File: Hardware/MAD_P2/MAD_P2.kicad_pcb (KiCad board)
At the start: 2 copper layers, 121.6 x 145.5 mm, 363 parts, among them J1 Line_1_3, J10 Conn_02x05_Odd_Even, J11 Conn_02x05_Odd_Even, J12 Line_3_3, J13 Conn_02x05_Odd_Even, J14 Conn_02x05_Odd_Even, J15 Conn_ADC1, J16 Conn_DAC, J17 Line_1_2, J18 P3, J19 P4, J2 Line_2_2, J20 P2, J21 Conn_02x05_Odd_Even, J22 Conn_02x05_Odd_Even, J23 Conn_02x03_Odd_Even, J24 P5, J25 P6, J26 P7, J27 Line_1_1, J28 Line_2_1, J29 Line_2_3, J3 Line_3_1, J30 Line_3_2, J31 Micro_SD_Card_Connector, J32 Micro_SD_Card_Socket, J33 Shifted IO, J4 Power_In, J5 Micro_SD_Card, J6 Edge_Conn, J7 Conn_02x05_Odd_Even, J8 USB_C_Receptacle_USB2.0, J9 Conn_02x05_Odd_Even, P10 CONN_01X01, P11 CONN_01X01, P13 CONN_01X01, P8 CONN_01X01, Q1 MMBT3904, Q2 2N7002, Q3 2N7002, Q4 2N7002, Q5 2N7002, SW1 Switch_SW_Push, U1 P2X8C4M64P-REF, U10 AMS1117-3.3, U11 APM4953, U12 APM4953, U13 XL1509-5.0, U14 XL1509-5.0, U15 AMS1117-3.3, U16 AMS1117-3.3, U17 MAX5134-7, U18 AMS1117-3.3, U19 AMS1117-1.8, U2 XL1509-5.0, U20 LM321, U21 APM4953, U22 XL1509-5.0, U23 ADS131A04, U24 AMS1117-3.3, U26 W25Q128JVS, U27 FT232RL, U28 DS3231M, U29 ESP-12F, U3 XL1509-5.0, U4 XL1509-5.0, U5 XL1509-5.0, U6 AMS1117-3.3, U7 AMS1117-3.3, U8 AMS1117-3.3, U9 AMS1117-3.3, Y1 20MHz, Y2 16.384MHz

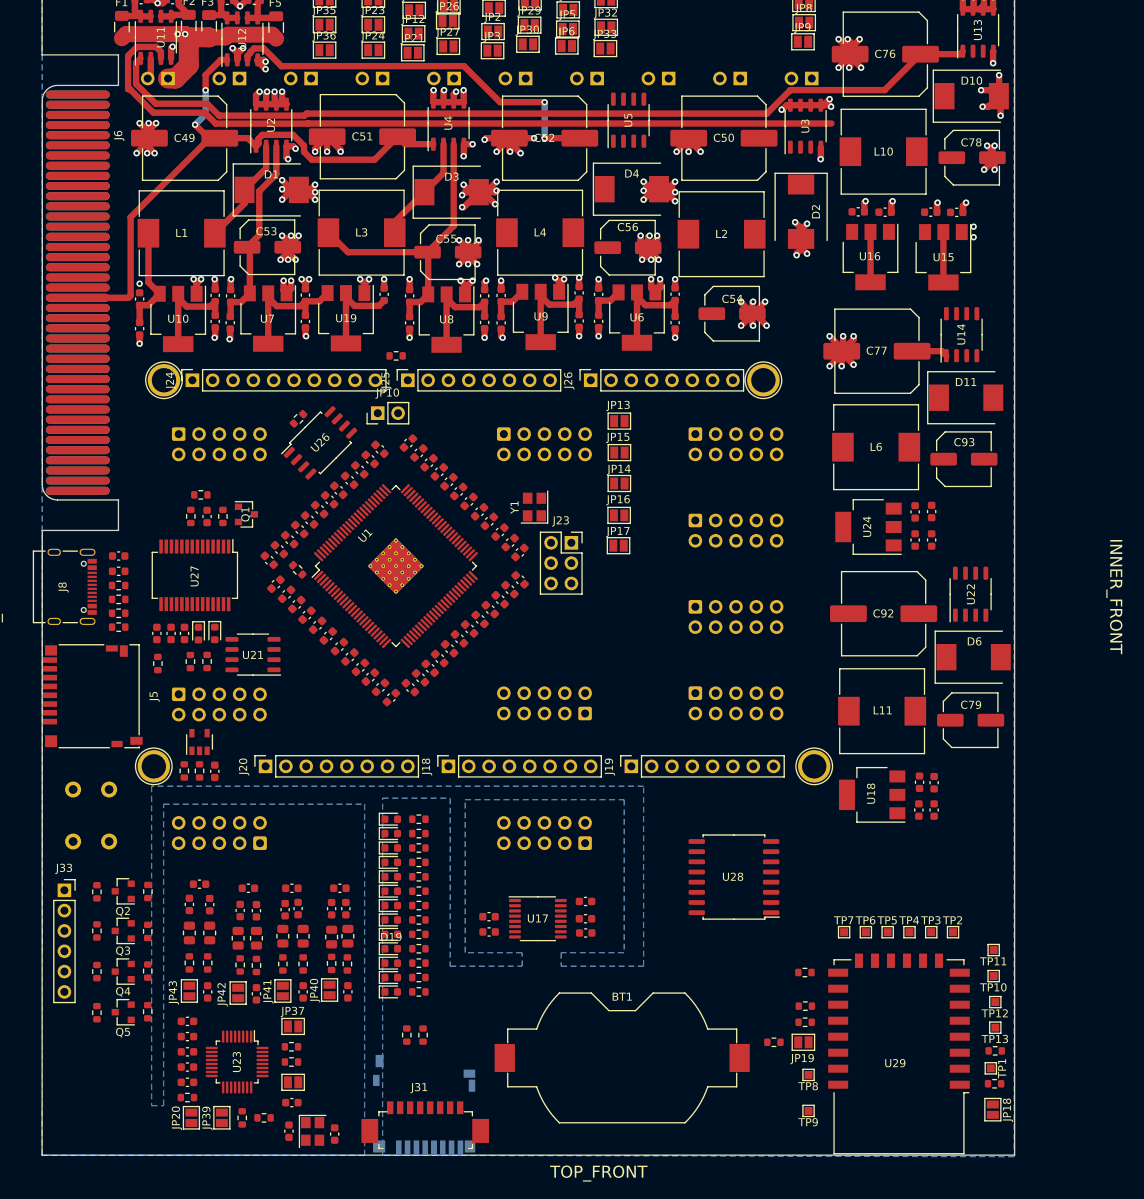
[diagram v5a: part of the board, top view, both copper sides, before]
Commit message: routed adc
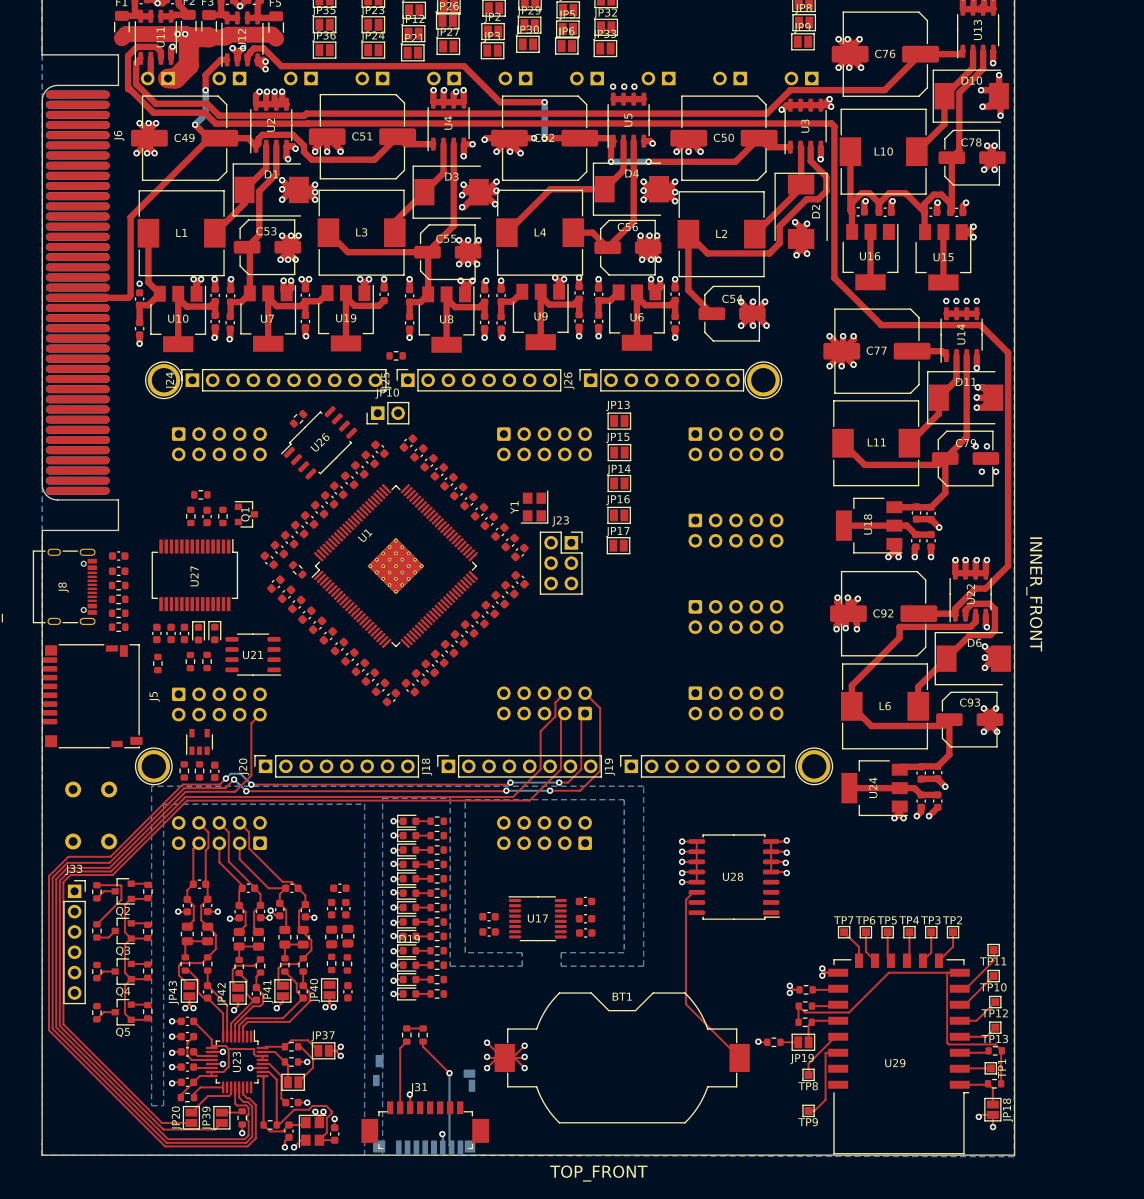
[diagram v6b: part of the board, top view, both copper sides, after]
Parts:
- moved C82 33.7 mm to (501.6, 84.1)
- moved C83 33.7 mm to (501.7, 80.6)
- moved C86 33.7 mm to (503.6, 84.1)
- moved C87 33.7 mm to (503.6, 80.7)
- moved U18 33.7 mm to (495.8, 82.2)
- moved L11 33.5 mm to (496.7, 71.9)
- moved C79 32.7 mm to (507.9, 73.8)
- moved C100 32.6 mm to (504.4, 116.6)
- moved C101 32.6 mm to (502.3, 116.6)
- moved C95 32.6 mm to (504.4, 113.1)
- moved C97 32.6 mm to (502.3, 113.1)
- moved U24 32.6 mm to (496.5, 115.0)
- moved C93 32.6 mm to (508.4, 106.4)
- moved L6 32.4 mm to (497.8, 104.8)
- moved JP37 4.88 mm to (427.6, 147.8)
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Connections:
- net /Connections/P64 renamed Net-(J11-Pad1)
- net D+ renamed /Connections/D+
- net D- renamed /Connections/D-
- C1 pad 1: /V_0_3 -> V_0_3
- C10 pad 1: /V_36_39 -> V_32_35
- C13 pad 1: /V_8_11 -> V_0_3
- C14 pad 1: /V_8_11 -> V_0_3
- C15 pad 1: /V_40_43 -> V_32_35
- C16 pad 1: /V_40_43 -> V_32_35
- C19 pad 1: /V_12_15 -> V_0_3
- C2 pad 1: /V_0_3 -> V_0_3
- C20 pad 1: /V_12_15 -> V_0_3
- C21 pad 1: /V_44_47 -> V_32_35
- C22 pad 1: /V_44_47 -> V_32_35
- C25 pad 1: /V_16_19 -> V_0_3
- C26 pad 1: /V_16_19 -> V_0_3
- C27 pad 1: /V_48_51 -> V_32_35
- C28 pad 1: /V_48_51 -> V_32_35
- C3 pad 1: /V_32_35 -> V_32_35
- C31 pad 1: /V_20_23 -> V_0_3
- C32 pad 1: /V_20_23 -> V_0_3
- C33 pad 1: /V_52_55 -> V_32_35
- C34 pad 1: /V_52_55 -> V_32_35
- C37 pad 1: /V_24_27 -> V_0_3
- C38 pad 1: /V_24_27 -> V_0_3
- C39 pad 1: /V_56_59 -> V_32_35
- C4 pad 1: /V_32_35 -> V_32_35
- C40 pad 1: /V_56_59 -> V_32_35
- C43 pad 1: /V_28_31 -> V_0_3
- C44 pad 1: /V_28_31 -> V_0_3
- C45 pad 1: /V_60_63 -> V_32_35
- C46 pad 1: /V_60_63 -> V_32_35
- C7 pad 1: /V_4_7 -> V_0_3
- C8 pad 1: /V_4_7 -> V_0_3
- C9 pad 1: /V_36_39 -> V_32_35
- J10 pad 1: /Connections/P54 -> P54
- J10 pad 10: /Connections/P63 -> P63
- J10 pad 2: /Connections/P55 -> P55
- J10 pad 3: /Connections/P56 -> P56
- J10 pad 4: /Connections/P57 -> P57
- J10 pad 5: /Connections/P58 -> P58
- J10 pad 6: /Connections/P59 -> P59
- J10 pad 7: /Connections/P60 -> P60
- J10 pad 8: /Connections/P61 -> P61
- J10 pad 9: /Connections/P62 -> P62
- J11 pad 2: /Connections/V_0_3 -> V_0_3
- J11 pad 3: /Connections/V_16_19 -> V_0_3
- J11 pad 4: /Connections/V_32_35 -> V_32_35
- J11 pad 5: /Connections/V_48_51 -> V_32_35
- J13 pad 1: /Connections/P20 -> P20
- J13 pad 10: /Connections/P29 -> P29
- J13 pad 2: /Connections/P21 -> P21
- J13 pad 3: /Connections/P22 -> P22
- J13 pad 4: /Connections/P23 -> P23
- J13 pad 5: /Connections/P24 -> P24
- J13 pad 6: /Connections/P25 -> P25
- J13 pad 7: /Connections/P26 -> P26
- J13 pad 8: /Connections/P27 -> P27
- J13 pad 9: /Connections/P28 -> P28
- J16 pad 10: /Connections/A03 -> AO3
- J16 pad 2: /Connections/A01 -> AO1
- J16 pad 5: /Connections/A02 -> AO2
- J21 pad 1: /Connections/P0 -> P0
- J21 pad 10: /Connections/P9 -> P9
- J21 pad 2: /Connections/P1 -> P1
- J21 pad 3: /Connections/P2 -> P2
- J21 pad 4: /Connections/P3 -> P3
- J21 pad 5: /Connections/P4 -> P4
- J21 pad 6: /Connections/P5 -> P5
- J21 pad 7: /Connections/P6 -> P6
- J21 pad 8: /Connections/P7 -> P7
- J21 pad 9: /Connections/P8 -> P8
- J22 pad 1: /Connections/P10 -> P10
- J22 pad 10: /Connections/P19 -> P19
- J22 pad 2: /Connections/P11 -> P11
- J22 pad 3: /Connections/P12 -> P12
- J22 pad 4: /Connections/P13 -> P13
- J22 pad 5: /Connections/P14 -> P14
- J22 pad 6: /Connections/P15 -> P15
- J22 pad 7: /Connections/P16 -> P16
- J22 pad 8: /Connections/P17 -> P17
- J22 pad 9: /Connections/P18 -> P18
- J23 pad 2: /Connections/P53 -> P53
- J23 pad 3: /Connections/P52 -> P52
- J23 pad 4: /Connections/P51 -> P51
- J24 pad 8: /Connections/P55 -> P55
- J24 pad 9: /Connections/P54 -> P54
- J26 pad 7: /Connections/P57 -> P57
- J26 pad 8: /Connections/P56 -> P56
- J31 pad 2: /Connections/P42 -> P42
- J31 pad 3: /Connections/P41 -> P41
- J31 pad 5: /Connections/P40 -> P40
- J32 pad 2: /Connections/P42 -> P42
- J32 pad 3: /Connections/P41 -> P41
- J32 pad 5: /Connections/P40 -> P40
- J5 pad 2: /Memory/P60 -> P60
- J5 pad 3: /Memory/P59 -> P59
- J5 pad 5: /Memory/P61 -> P61
- J6 pad 10: /Connections/P30 -> P30
- J6 pad 11: /Connections/P29 -> P29
- J6 pad 12: /Connections/P28 -> P28
- J6 pad 13: /Connections/P27 -> P27
- J6 pad 14: /Connections/P26 -> P26
- J6 pad 15: /Connections/P25 -> P25
- J6 pad 16: /Connections/P24 -> P24
- J6 pad 17: /Connections/P23 -> P23
- J6 pad 18: /Connections/P22 -> P22
- J6 pad 19: /Connections/P21 -> P21
- J6 pad 20: /Connections/P20 -> P20
- J6 pad 21: /Connections/P19 -> P19
- J6 pad 22: /Connections/P18 -> P18
- J6 pad 23: /Connections/P17 -> P17
- J6 pad 24: /Connections/P16 -> P16
- J6 pad 25: /Connections/P15 -> P15
- J6 pad 26: /Connections/P14 -> P14
- J6 pad 27: /Connections/P13 -> P13
- J6 pad 28: /Connections/P12 -> P12
- J6 pad 29: /Connections/P11 -> P11
- J6 pad 3: /Connections/P37 -> P37
- J6 pad 30: /Connections/P10 -> P10
- J6 pad 31: /Connections/P9 -> P9
- J6 pad 32: /Connections/P8 -> P8
- J6 pad 33: /Connections/P7 -> P7
- J6 pad 34: /Connections/P6 -> P6
- J6 pad 35: /Connections/P5 -> P5
- J6 pad 36: /Connections/P4 -> P4
- J6 pad 37: /Connections/P3 -> P3
- J6 pad 38: /Connections/P2 -> P2
- J6 pad 39: /Connections/P1 -> P1
- J6 pad 4: /Connections/P36 -> P36
- J6 pad 40: /Connections/P0 -> P0
- J6 pad 47: /Connections/V_0_3 -> V_0_3
- J6 pad 48: /Connections/V_8_11 -> V_0_3
- J6 pad 49: /Connections/P63 -> P63
- J6 pad 5: /Connections/P35 -> P35
- J6 pad 50: /Connections/P62 -> P62
- J6 pad 51: /Connections/P61 -> P61
- J6 pad 52: /Connections/P60 -> P60
- J6 pad 53: /Connections/P59 -> P59
- J6 pad 54: /Connections/P58 -> P58
- J6 pad 55: /Connections/P57 -> P57
- J6 pad 56: /Connections/P56 -> P56
- J6 pad 57: /Connections/V_56_59 -> V_32_35
- J6 pad 58: /Connections/V_16_19 -> V_0_3
- J6 pad 59: /Connections/P55 -> P55
- J6 pad 6: /Connections/P34 -> P34
- J6 pad 60: /Connections/P54 -> P54
- J6 pad 61: /Connections/P53 -> P53
- J6 pad 62: /Connections/P52 -> P52
- J6 pad 63: /Connections/P51 -> P51
- J6 pad 64: /Connections/P50 -> P50
- J6 pad 65: /Connections/P49 -> P49
- J6 pad 66: /Connections/P48 -> P48
- J6 pad 67: /Connections/V_48_51 -> V_32_35
- J6 pad 68: /Connections/V_24_27 -> V_0_3
- J6 pad 69: /Connections/P47 -> P47
- J6 pad 7: /Connections/P33 -> P33
- J6 pad 70: /Connections/P46 -> P46
- J6 pad 71: /Connections/P45 -> P45
- J6 pad 72: /Connections/P44 -> P44
- J6 pad 73: /Connections/P43 -> P43
- J6 pad 74: /Connections/P42 -> P42
- J6 pad 75: /Connections/P41 -> P41
- J6 pad 76: /Connections/P40 -> P40
- J6 pad 77: /Connections/V_40_43 -> V_32_35
- J6 pad 78: /Connections/V_32_35 -> V_32_35
- J6 pad 79: /Connections/P39 -> P39
- J6 pad 8: /Connections/P32 -> P32
- J6 pad 80: /Connections/P38 -> P38
- J6 pad 9: /Connections/P31 -> P31
- J7 pad 1: /Connections/P34 -> P34
- J7 pad 10: /Connections/P43 -> P43
- J7 pad 2: /Connections/P35 -> P35
- J7 pad 3: /Connections/P36 -> P36
- J7 pad 4: /Connections/P37 -> P37
- J7 pad 5: /Connections/P38 -> P38
- J7 pad 6: /Connections/P39 -> P39
- J7 pad 7: /Connections/P40 -> P40
- J7 pad 8: /Connections/P41 -> P41
- J7 pad 9: /Connections/P42 -> P42
- J9 pad 1: /Connections/P44 -> P44
- J9 pad 10: /Connections/P53 -> P53
- J9 pad 2: /Connections/P45 -> P45
- J9 pad 3: /Connections/P46 -> P46
- J9 pad 4: /Connections/P47 -> P47
- J9 pad 5: /Connections/P48 -> P48
- J9 pad 6: /Connections/P49 -> P49
- J9 pad 7: /Connections/P50 -> P50
- J9 pad 8: /Connections/P51 -> P51
- J9 pad 9: /Connections/P52 -> P52
- JP10 pad 2: /Memory/P61 -> P61
- JP13 pad 2: /Connections/P30 -> P30
- JP14 pad 2: /Connections/P32 -> P32
- JP15 pad 1: /Connections/P31 -> P31
- JP16 pad 2: /Connections/P33 -> P33
- JP17 pad 1: /Connections/P34 -> P34
- JP20 pad 2: /Peripherals/P46 -> P46
- JP39 pad 2: /Peripherals/P47 -> P47
- Q2 pad 2: /Peripherals/P51 -> P51
- Q3 pad 2: /Peripherals/P52 -> P52
- Q4 pad 2: /Peripherals/P53 -> P53
- Q5 pad 2: /Peripherals/P54 -> P54
- R11 pad 1: /Memory/P58 -> P58
- R18 pad 2: /Connections/P63 -> P63
- R19 pad 1: /Connections/P62 -> P62
- R2 pad 1: /V_56_59 -> V_32_35
- R2 pad 2: /RESET -> RESET
- R35 pad 1: /Connections/P39 -> P39
- R36 pad 1: /Connections/P39 -> P39
- R38 pad 2: /Peripherals/P51 -> P51
- R43 pad 2: /Peripherals/P52 -> P52
- R48 pad 2: /Peripherals/P53 -> P53
- R50 pad 2: /Peripherals/P54 -> P54
- SW1 pad 1: /RESET -> RESET
- U1 pad 10: /P5 -> P5
- U1 pad 100: /RESET -> RESET
- U1 pad 11: /V_4_7 -> V_0_3
- U1 pad 12: /P6 -> P6
- U1 pad 13: /P7 -> P7
- U1 pad 15: /P8 -> P8
- U1 pad 16: /P9 -> P9
- U1 pad 17: /V_8_11 -> V_0_3
- U1 pad 18: /P10 -> P10
- U1 pad 19: /P11 -> P11
- U1 pad 21: /P12 -> P12
- U1 pad 22: /P13 -> P13
- U1 pad 23: /V_12_15 -> V_0_3
- U1 pad 24: /P14 -> P14
- U1 pad 25: /P15 -> P15
- U1 pad 27: /P16 -> P16
- U1 pad 28: /P17 -> P17
- U1 pad 29: /V_16_19 -> V_0_3
- U1 pad 3: /P0 -> P0
- U1 pad 30: /P18 -> P18
- U1 pad 31: /P19 -> P19
- U1 pad 33: /P20 -> P20
- U1 pad 34: /P21 -> P21
- U1 pad 35: /V_20_23 -> V_0_3
- U1 pad 36: /P22 -> P22
- U1 pad 37: /P23 -> P23
- U1 pad 39: /P24 -> P24
- U1 pad 4: /P1 -> P1
- U1 pad 40: /P25 -> P25
- U1 pad 41: /V_24_27 -> V_0_3
- U1 pad 42: /P26 -> P26
- U1 pad 43: /P27 -> P27
- U1 pad 45: /P28 -> P28
- U1 pad 46: /P29 -> P29
- U1 pad 47: /V_28_31 -> V_0_3
- U1 pad 48: /P30 -> P30
- U1 pad 49: /P31 -> P31
- U1 pad 5: /V_0_3 -> V_0_3
- U1 pad 53: /P32 -> P32
- U1 pad 54: /P33 -> P33
- U1 pad 55: /V_32_35 -> V_32_35
- U1 pad 56: /P34 -> P34
- U1 pad 57: /P35 -> P35
- U1 pad 59: /P36 -> P36
- U1 pad 6: /P2 -> P2
- U1 pad 60: /P37 -> P37
- U1 pad 61: /V_36_39 -> V_32_35
- U1 pad 62: /P38 -> P38
- U1 pad 63: /P39 -> P39
- U1 pad 65: /P40 -> P40
- U1 pad 66: /P41 -> P41
- U1 pad 67: /V_40_43 -> V_32_35
- U1 pad 68: /P42 -> P42
- U1 pad 69: /P43 -> P43
- U1 pad 7: /P3 -> P3
- U1 pad 71: /P44 -> P44
- U1 pad 72: /P45 -> P45
- U1 pad 73: /V_44_47 -> V_32_35
- U1 pad 74: /P46 -> P46
- U1 pad 75: /P47 -> P47
- U1 pad 77: /P48 -> P48
- U1 pad 78: /P49 -> P49
- U1 pad 79: /V_48_51 -> V_32_35
- U1 pad 80: /P50 -> P50
- U1 pad 81: /P51 -> P51
- U1 pad 83: /P52 -> P52
- U1 pad 84: /P53 -> P53
- U1 pad 85: /V_52_55 -> V_32_35
- U1 pad 86: /P54 -> P54
- U1 pad 87: /P55 -> P55
- U1 pad 89: /P56 -> P56
- U1 pad 9: /P4 -> P4
- U1 pad 90: /P57 -> P57
- U1 pad 91: /V_56_59 -> V_32_35
- U1 pad 92: /P58 -> P58
- U1 pad 93: /P59 -> P59
- U1 pad 95: /P60 -> P60
- U1 pad 96: /P61 -> P61
- U1 pad 97: /V_60_63 -> V_32_35
- U1 pad 98: /P62 -> P62
- U1 pad 99: /P63 -> P63
- U15 pad 2: /Power2/V_0_3 -> V_0_3
- U16 pad 2: /Power2/V_16_19 -> V_32_35
- U17 pad 10: /Peripherals/P49 -> P49
- U17 pad 11: /Peripherals/A02 -> AO2
- U17 pad 14: /Peripherals/A01 -> AO1
- U17 pad 6: /Peripherals/A03 -> AO3
- U17 pad 8: /Peripherals/P50 -> P50
- U17 pad 9: /Peripherals/P48 -> P48
- U23 pad 20: /Peripherals/P43 -> P43
- U23 pad 21: /Peripherals/P45 -> P45
- U23 pad 22: /Peripherals/P44 -> P44
- U26 pad 2: /Memory/P58 -> P58
- U26 pad 5: /Memory/P59 -> P59
- U26 pad 6: /Memory/P60 -> P60
- U28 pad 15: /Peripherals/P37 -> P37
- U28 pad 16: /Peripherals/P38 -> P38
- U29 pad 21: /Peripherals/P35 -> P35
- U29 pad 22: /Peripherals/P36 -> P36
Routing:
- net GND: track 295.9 -> 489.3 mm, vias 151 -> 262
- net P45: track 0.00 -> 142.9 mm, vias 0 -> 4
- net P44: track 0.00 -> 139.1 mm, vias 0 -> 4
- net P47: track 0.00 -> 120.8 mm
- net P46: track 0.00 -> 114.2 mm
- net P43: track 0.00 -> 94.8 mm
- net VIN_ADC: track 99.5 -> 185.5 mm
- net +3V3: track 13.9 -> 85.6 mm
- net Net-(C78-Pad1): track 0.00 -> 55.7 mm
- net 5V_ADC: track 0.00 -> 47.9 mm
- net +5V_3: track 4.74 -> 44.9 mm
- net 3.3V_ADC: track 0.00 -> 39.9 mm
- net 5V_MAIN1: track 0.00 -> 39.6 mm
- net VIN_L2: track 49.8 -> 80.9 mm, vias 2 -> 4
- net A2-: track 0.00 -> 28.4 mm
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
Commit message: test
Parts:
- BT1: moved to B.Cu
- moved C119 2.26 mm to (428.2, 129.9)
- moved R39 2.26 mm to (428.3, 136.8)
- moved R62 2.26 mm to (428.4, 133.3)
- moved C122 2.07 mm to (430.7, 130.2)
- moved R40 2.07 mm to (430.7, 137.1)
- moved R57 2.07 mm to (430.7, 133.8)
- turned C120 to 90 degrees
- turned C121 to 0 degrees
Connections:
- J16 pad 3: 3.3V_ADC -> 5V_ADC
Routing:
- net 3.3V_ADC: track 39.9 -> 138.6 mm
- net A1-: track 0.00 -> 30.8 mm
- net 5V_ADC: track 47.9 -> 71.5 mm
- net HS_VIN: track 9.16 -> 31.0 mm
- net /Peripherals/AIN1P: track 0.00 -> 19.9 mm
- net /Peripherals/AIN1N: track 0.00 -> 19.6 mm
- net A1+: track 0.00 -> 17.3 mm
- net AO3: track 0.00 -> 15.8 mm
- net +3V3: track 85.6 -> 100.5 mm
- net AO1: track 0.00 -> 13.6 mm
- net AO2: track 0.00 -> 12.6 mm
- net Net-(JP39-Pad1): track 2.61 -> 12.3 mm, vias 0 -> 2
- net HS_4: track 2.65 -> 9.65 mm
- net HS_3: track 2.63 -> 7.02 mm
- net Net-(R39-Pad1): track 0.00 -> 4.24 mm
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
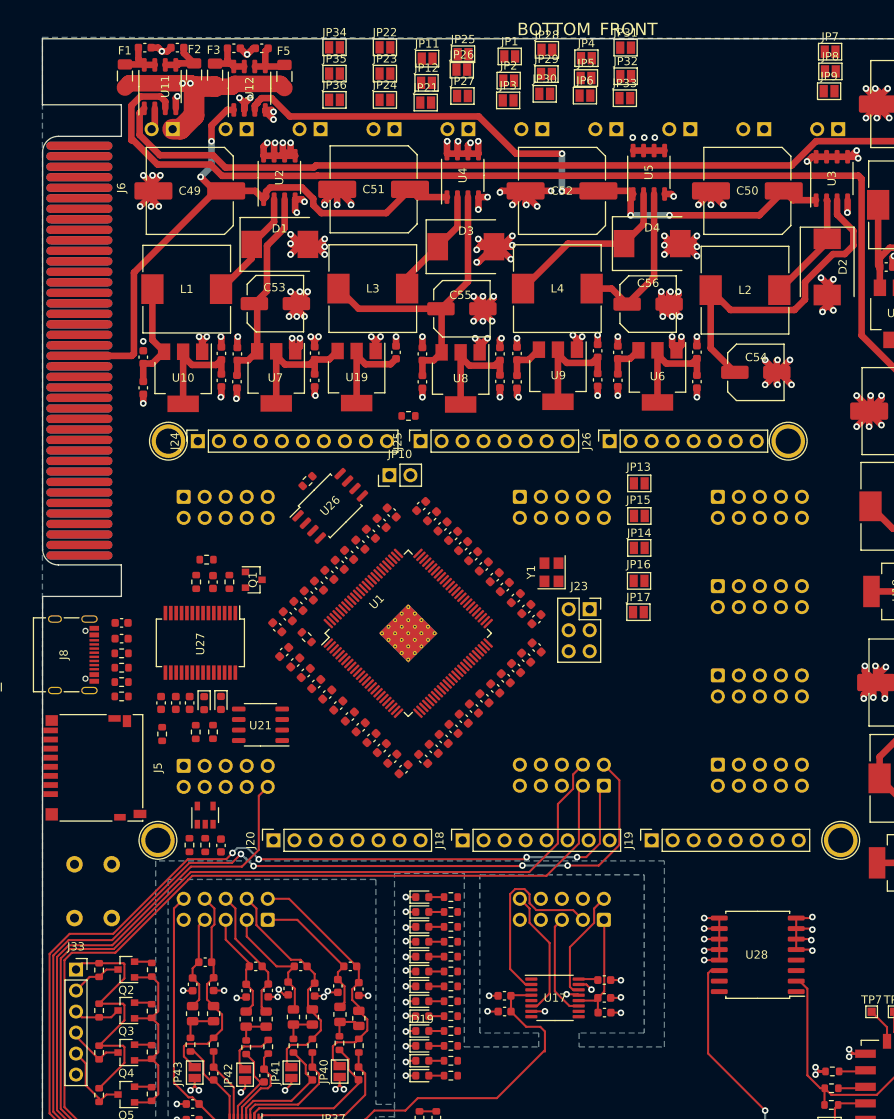
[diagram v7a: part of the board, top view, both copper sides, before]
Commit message: finished routing ground plane
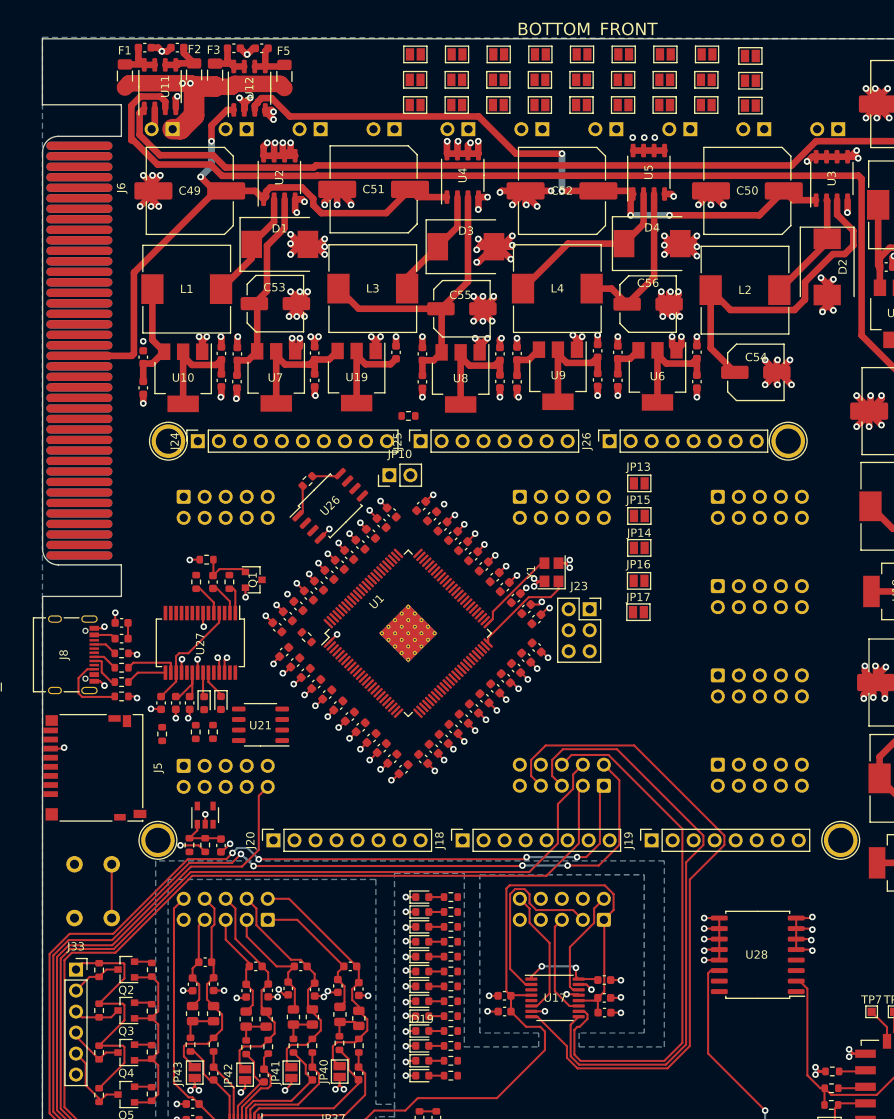
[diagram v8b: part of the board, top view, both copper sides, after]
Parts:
- moved JP34 12.0 mm to (437.5, 23.4)
- moved JP31 12.0 mm to (472.7, 23.4)
- moved JP7 11.6 mm to (478.0, 23.4)
- moved JP28 11.4 mm to (462.6, 23.4)
- moved JP33 11.3 mm to (472.8, 17.2)
- moved JP36 11.2 mm to (437.5, 17.2)
- moved JP22 11.1 mm to (442.5, 23.4)
- moved JP25 11.1 mm to (452.6, 23.4)
- moved JP4 11.0 mm to (467.7, 23.4)
- moved JP6 10.9 mm to (467.7, 17.2)
- moved JP27 10.7 mm to (452.6, 17.2)
- moved JP30 10.7 mm to (462.7, 17.2)
- moved JP21 10.6 mm to (447.6, 17.2)
- moved JP3 10.5 mm to (457.7, 17.2)
- moved JP1 10.5 mm to (457.6, 23.4)
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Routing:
- net GND: track 486.3 -> 579.2 mm, vias 265 -> 338
- net P50: track 0.00 -> 83.1 mm
- net P48: track 0.00 -> 73.4 mm
- net P49: track 0.00 -> 65.8 mm
- net 3.3V_ADC: track 138.6 -> 168.7 mm
- net Net-(C104-Pad1): track 0.00 -> 13.7 mm
- net Net-(U1-Pad50): track 0.00 -> 12.5 mm
- net Net-(U1-Pad51): track 0.00 -> 10.3 mm
- net VBUS: track 0.00 -> 8.93 mm
- net Net-(J8-PadB5): track 0.00 -> 8.78 mm
- net Net-(C94-Pad1): track 2.37 -> 10.1 mm, vias 0 -> 2
- net /Connections/D-: track 0.00 -> 6.53 mm
- net RESET: track 0.00 -> 6.50 mm
- net Net-(C107-Pad1): track 0.00 -> 6.35 mm
- net Net-(C90-Pad1): track 0.00 -> 5.94 mm
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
